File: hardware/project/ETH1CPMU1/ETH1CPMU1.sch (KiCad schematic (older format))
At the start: 0 parts

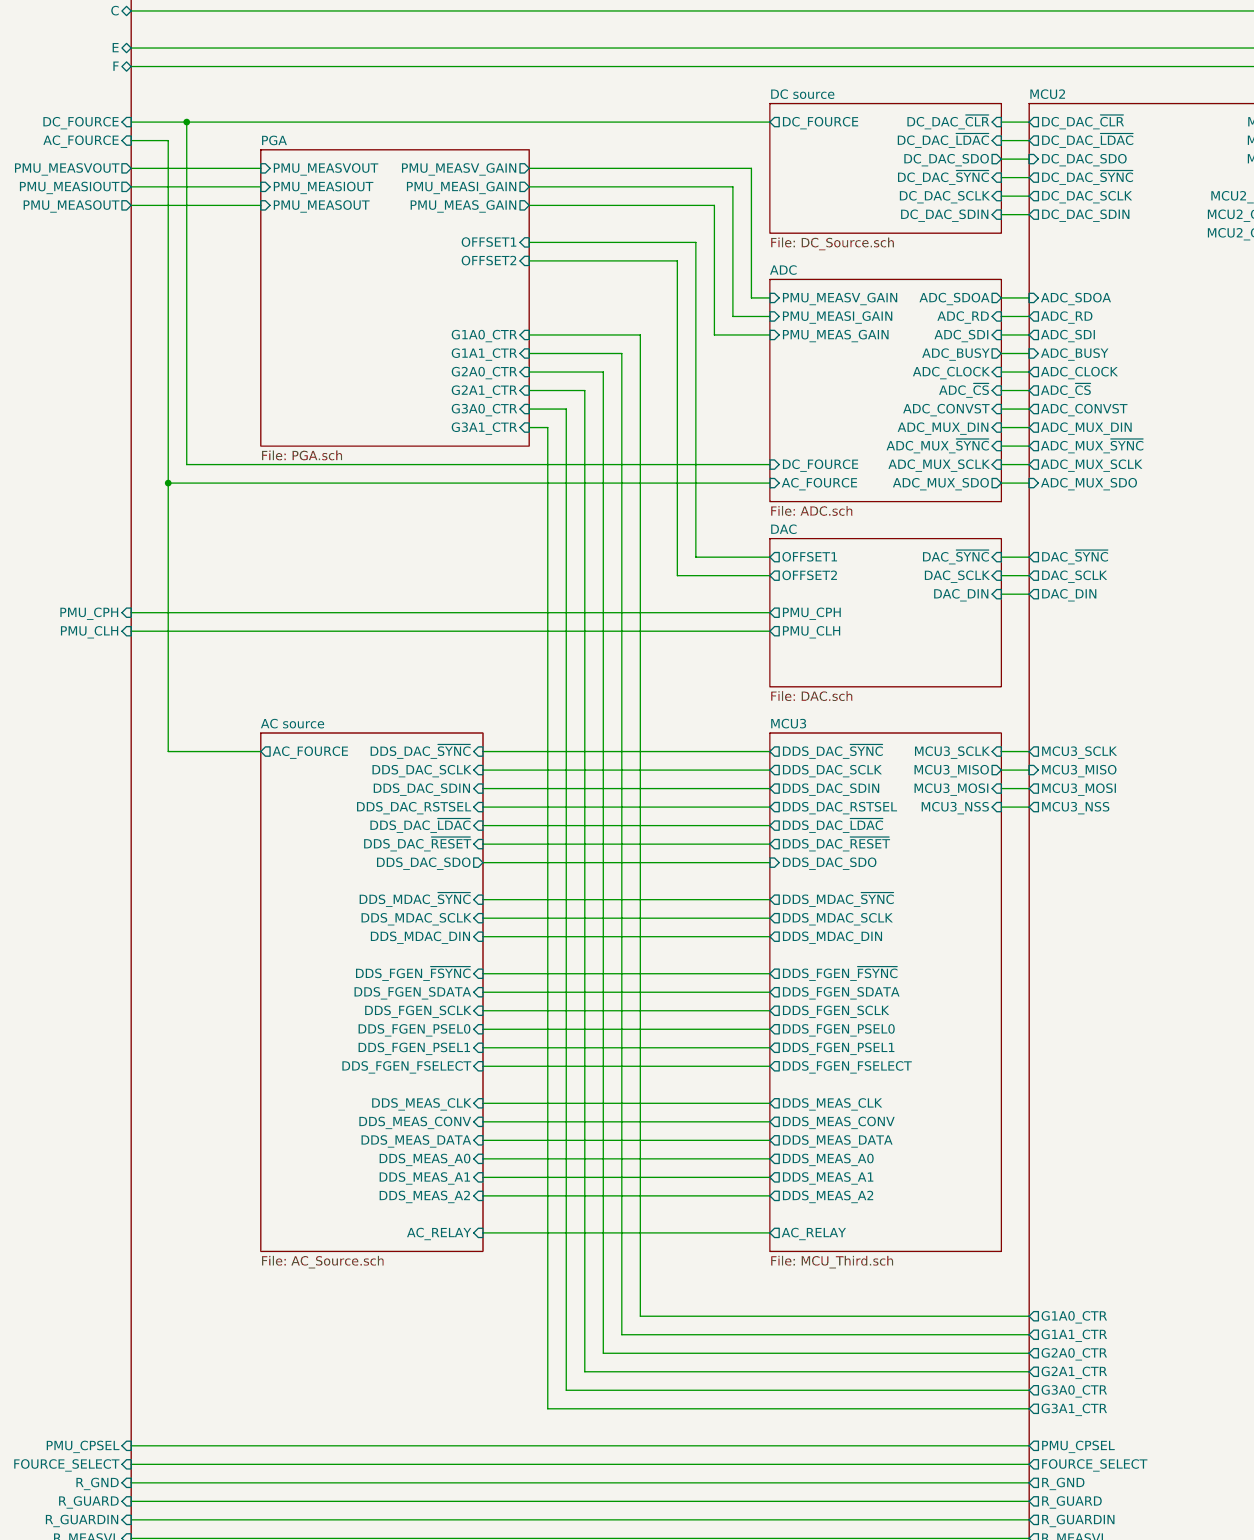
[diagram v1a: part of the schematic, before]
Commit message: Added two analog switches
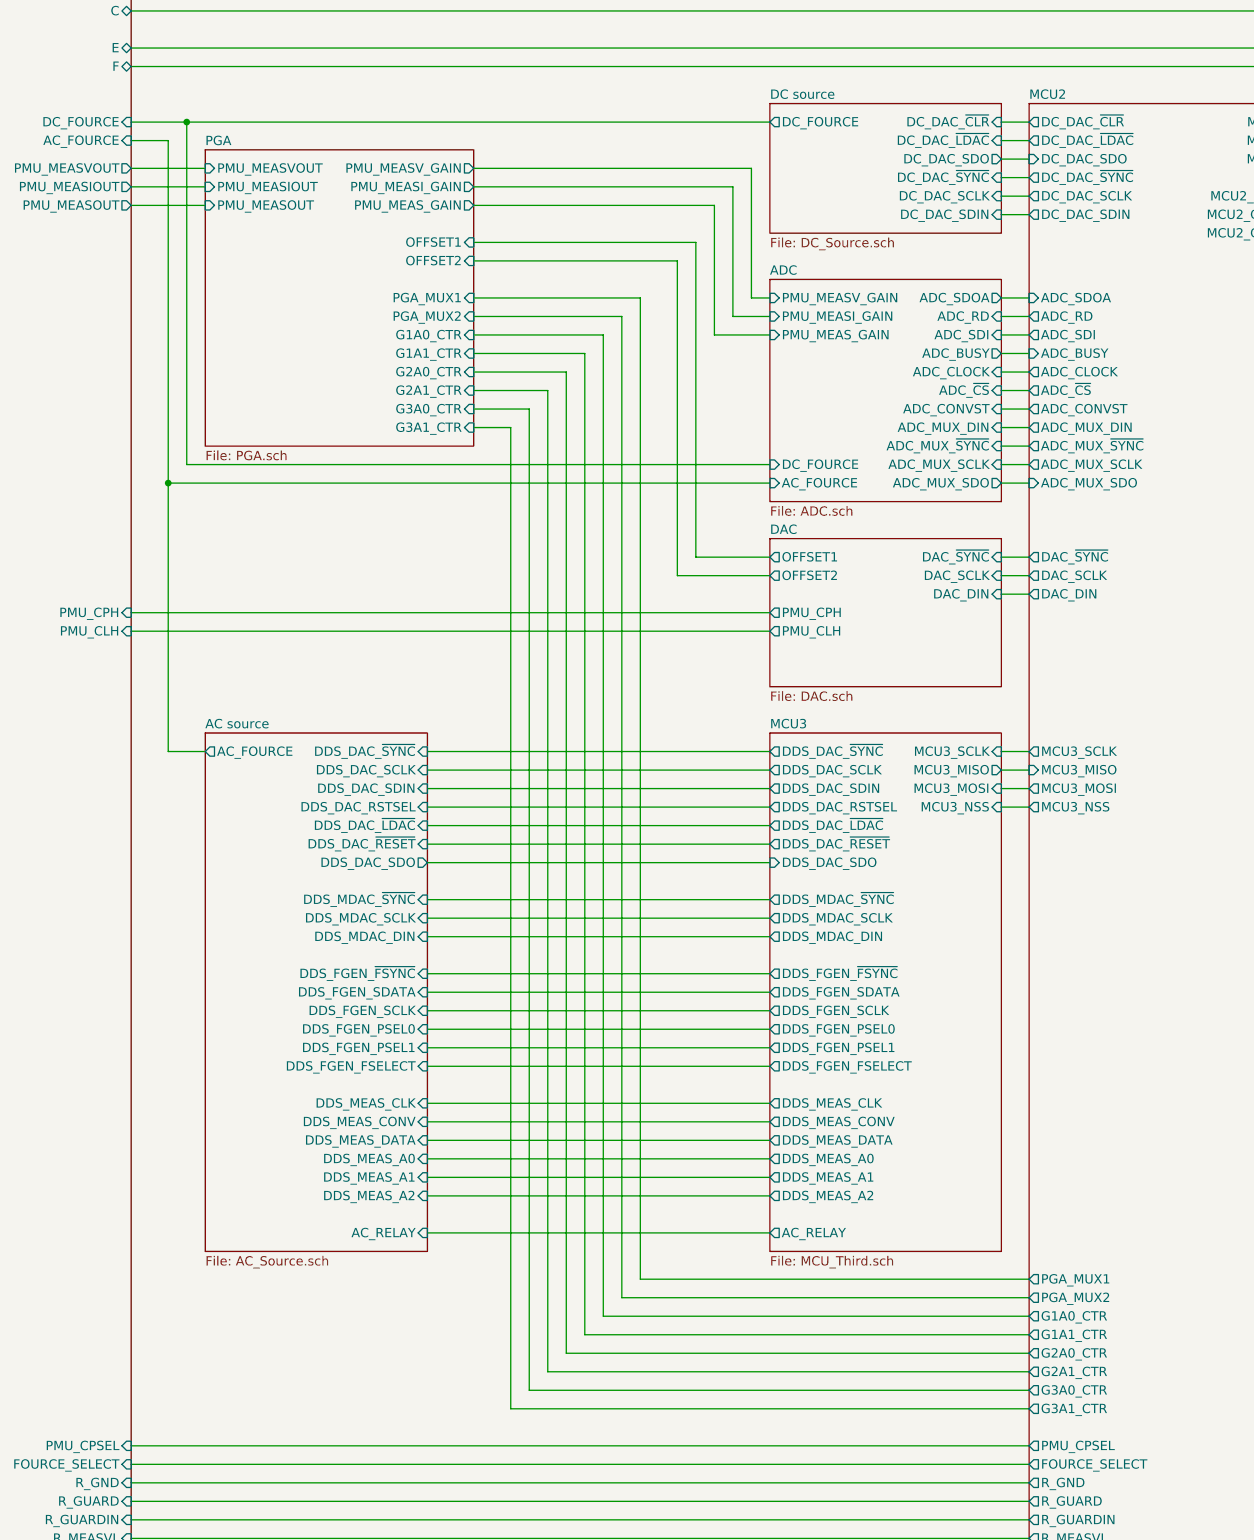
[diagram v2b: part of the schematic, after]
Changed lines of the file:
@@
 $EndSheet
 Wire Wire Line
-	4950 6650 6500 6650
-Wire Wire Line
-	6500 5550 4950 5550
-Wire Wire Line
-	4950 7350 6500 7350
-Wire Wire Line
-	6500 7250 4950 7250
-Wire Wire Line
-	4950 7150 6500 7150
-Wire Wire Line
-	6500 7050 4950 7050
-Wire Wire Line
-	4950 6950 6500 6950
-Wire Wire Line
-	6500 6850 4950 6850
-Wire Wire Line
-	6500 6350 4950 6350
-Wire Wire Line
-	6500 6550 4950 6550
-Wire Wire Line
-	4950 6450 6500 6450
-Wire Wire Line
-	6500 6250 4950 6250
-Wire Wire Line
-	4950 6150 6500 6150
-Wire Wire Line
-	6500 5250 4950 5250
-Wire Wire Line
-	4950 5350 6500 5350
-Wire Wire Line
-	6500 5450 4950 5450
-Wire Wire Line
-	4950 5950 6500 5950
-Wire Wire Line
-	6500 5850 4950 5850
-Wire Wire Line
-	4950 5750 6500 5750
-Wire Wire Line
-	6500 5150 4950 5150
-Wire Wire Line
-	4950 5050 6500 5050
-Wire Wire Line
-	6500 4950 4950 4950
-Wire Wire Line
-	3750 4950 3250 4950
+	4650 6650 6500 6650
+Wire Wire Line
+	6500 5550 4650 5550
+Wire Wire Line
+	4650 7350 6500 7350
+Wire Wire Line
+	6500 7250 4650 7250
+Wire Wire Line
+	4650 7150 6500 7150
+Wire Wire Line
+	6500 7050 4650 7050
+Wire Wire Line
+	4650 6950 6500 6950
+Wire Wire Line
+	6500 6850 4650 6850
+Wire Wire Line
+	6500 6350 4650 6350
+Wire Wire Line
+	6500 6550 4650 6550
+Wire Wire Line
+	4650 6450 6500 6450
+Wire Wire Line
+	6500 6250 4650 6250
+Wire Wire Line
+	4650 6150 6500 6150
+Wire Wire Line
+	6500 5250 4650 5250
+Wire Wire Line
+	4650 5350 6500 5350
+Wire Wire Line
+	6500 5450 4650 5450
+Wire Wire Line
+	4650 5950 6500 5950
+Wire Wire Line
+	6500 5850 4650 5850
+Wire Wire Line
+	4650 5750 6500 5750
+Wire Wire Line
+	6500 5150 4650 5150
+Wire Wire Line
+	4650 5050 6500 5050
+Wire Wire Line
+	6500 4950 4650 4950
+Wire Wire Line
+	3450 4950 3250 4950
 $Sheet
-S 3750 4850 1200 2800
+S 3450 4850 1200 2800
 U 5DF36C25
 F0 "AC source" 50
 F1 "AC_Source.sch" 50
-F2 "AC_FOURCE" O L 3750 4950 50
-F3 "DDS_DAC_~SYNC" I R 4950 4950 50
-F4 "DDS_DAC_SCLK" I R 4950 5050 50
-F5 "DDS_DAC_SDIN" I R 4950 5150 50
-F6 "DDS_MDAC_~SYNC" I R 4950 5750 50
-F7 "DDS_MDAC_SCLK" I R 4950 5850 50
-F8 "DDS_MDAC_DIN" I R 4950 5950 50
-F9 "DDS_DAC_~RESET" I R 4950 5450 50
-F10 "DDS_DAC_~LDAC" I R 4950 5350 50
-F11 "DDS_DAC_RSTSEL" I R 4950 5250 50
-F12 "DDS_FGEN_~FSYNC" I R 4950 6150 50
-F13 "DDS_FGEN_SDATA" I R 4950 6250 50
-F14 "DDS_FGEN_PSEL0" I R 4950 6450 50
-F15 "DDS_FGEN_PSEL1" I R 4950 6550 50
-F16 "DDS_FGEN_SCLK" I R 4950 6350 50
-F17 "DDS_MEAS_CLK" I R 4950 6850 50
-F18 "DDS_MEAS_CONV" I R 4950 6950 50
-F19 "DDS_MEAS_DATA" I R 4950 7050 50
-F20 "DDS_MEAS_A0" I R 4950 7150 50
-F21 "DDS_MEAS_A1" I R 4950 7250 50
-F22 "DDS_MEAS_A2" I R 4950 7350 50
-F23 "DDS_DAC_SDO" O R 4950 5550 50
-F24 "DDS_FGEN_FSELECT" I R 4950 6650 50
-F25 "AC_RELAY" I R 4950 7550 50
+F2 "AC_FOURCE" O L 3450 4950 50
+F3 "DDS_DAC_~SYNC" I R 4650 4950 50
+F4 "DDS_DAC_SCLK" I R 4650 5050 50
+F5 "DDS_DAC_SDIN" I R 4650 5150 50
+F6 "DDS_MDAC_~SYNC" I R 4650 5750 50
+F7 "DDS_MDAC_SCLK" I R 4650 5850 50
+F8 "DDS_MDAC_DIN" I R 4650 5950 50
+F9 "DDS_DAC_~RESET" I R 4650 5450 50
+F10 "DDS_DAC_~LDAC" I R 4650 5350 50
+F11 "DDS_DAC_RSTSEL" I R 4650 5250 50
+F12 "DDS_FGEN_~FSYNC" I R 4650 6150 50
+F13 "DDS_FGEN_SDATA" I R 4650 6250 50
+F14 "DDS_FGEN_PSEL0" I R 4650 6450 50
+F15 "DDS_FGEN_PSEL1" I R 4650 6550 50
+F16 "DDS_FGEN_SCLK" I R 4650 6350 50
+F17 "DDS_MEAS_CLK" I R 4650 6850 50
+F18 "DDS_MEAS_CONV" I R 4650 6950 50
+F19 "DDS_MEAS_DATA" I R 4650 7050 50
+F20 "DDS_MEAS_A0" I R 4650 7150 50
+F21 "DDS_MEAS_A1" I R 4650 7250 50
+F22 "DDS_MEAS_A2" I R 4650 7350 50
+F23 "DDS_DAC_SDO" O R 4650 5550 50
+F24 "DDS_FGEN_FSELECT" I R 4650 6650 50
+F25 "AC_RELAY" I R 4650 7550 50
 $EndSheet
 Wire Wire Line
@@
 	3050 4300 6500 4300
 Wire Wire Line
-	6500 7550 4950 7550
+	6500 7550 4650 7550
 $Sheet
-S 3750 1700 1450 1600
+S 3450 1700 1450 1600
 U 5DED09C5
 F0 "PGA" 50
 F1 "PGA.sch" 50
-F2 "PMU_MEASV_GAIN" O R 5200 1800 50
-F3 "PMU_MEASI_GAIN" O R 5200 1900 50
-F4 "PMU_MEASVOUT" I L 3750 1800 50
-F5 "PMU_MEASIOUT" I L 3750 1900 50
-F6 "G1A0_CTR" I R 5200 2700 50
-F7 "G1A1_CTR" I R 5200 2800 50
-F8 "G2A0_CTR" I R 5200 2900 50
-F9 "G2A1_CTR" I R 5200 3000 50
-F10 "PMU_MEAS_GAIN" O R 5200 2000 50
-F11 "PMU_MEASOUT" I L 3750 2000 50
-F12 "G3A0_CTR" I R 5200 3100 50
-F13 "G3A1_CTR" I R 5200 3200 50
-F14 "OFFSET1" I R 5200 2200 50
-F15 "OFFSET2" I R 5200 2300 50
+F2 "PMU_MEASV_GAIN" O R 4900 1800 50
+F3 "PMU_MEASI_GAIN" O R 4900 1900 50
+F4 "PMU_MEASVOUT" I L 3450 1800 50
+F5 "PMU_MEASIOUT" I L 3450 1900 50
+F6 "G1A0_CTR" I R 4900 2700 50
+F7 "G1A1_CTR" I R 4900 2800 50
+F8 "G2A0_CTR" I R 4900 2900 50
+F9 "G2A1_CTR" I R 4900 3000 50
+F10 "PMU_MEAS_GAIN" O R 4900 2000 50
+F11 "PMU_MEASOUT" I L 3450 2000 50
+F12 "G3A0_CTR" I R 4900 3100 50
+F13 "G3A1_CTR" I R 4900 3200 50
+F14 "OFFSET1" I R 4900 2200 50
+F15 "OFFSET2" I R 4900 2300 50
+F16 "PGA_MUX1" I R 4900 2500 50
+F17 "PGA_MUX2" I R 4900 2600 50
 $EndSheet
 $Sheet
@@
 F60 "G2A0_CTR" O L 7900 8200 50
 F61 "G2A1_CTR" O L 7900 8300 50
+F62 "PGA_MUX1" O L 7900 7800 50
+F63 "PGA_MUX2" O L 7900 7900 50
 $EndSheet
 Wire Wire Line
@@
 	7900 3500 7750 3500
 Wire Wire Line
-	5200 1800 6400 1800
+	4900 1800 6400 1800
 Wire Wire Line
 	6400 1800 6400 2500
@@
 	6400 2500 6500 2500
 Wire Wire Line
-	5200 1900 6300 1900
+	4900 1900 6300 1900
 Wire Wire Line
 	6300 1900 6300 2600
@@
 	6300 2600 6500 2600
 Wire Wire Line
-	5200 2000 6200 2000
+	4900 2000 6200 2000
 Wire Wire Line
 	6200 2000 6200 2700
@@
 	6200 2700 6500 2700
 Wire Wire Line
-	3050 1800 3750 1800
-Wire Wire Line
-	3050 1900 3750 1900
-Wire Wire Line
-	3750 2000 3050 2000
-Wire Wire Line
-	7900 8000 5800 8000
-Wire Wire Line
-	5800 8000 5800 2700
-Wire Wire Line
-	5800 2700 5200 2700
-Wire Wire Line
-	7900 8100 5700 8100
-Wire Wire Line
-	5700 8100 5700 2800
-Wire Wire Line
-	5700 2800 5200 2800
-Wire Wire Line
-	7900 8200 5600 8200
-Wire Wire Line
-	5600 8200 5600 2900
-Wire Wire Line
-	5600 2900 5200 2900
-Wire Wire Line
-	7900 8300 5500 8300
-Wire Wire Line
-	5500 8300 5500 3000
-Wire Wire Line
-	5500 3000 5200 3000
-Wire Wire Line
-	7900 8400 5400 8400
-Wire Wire Line
-	5400 8400 5400 3100
-Wire Wire Line
-	5400 3100 5200 3100
-Wire Wire Line
-	7900 8500 5300 8500
-Wire Wire Line
-	5300 8500 5300 3200
-Wire Wire Line
-	5300 3200 5200 3200
+	3050 1800 3450 1800
+Wire Wire Line
+	3050 1900 3450 1900
+Wire Wire Line
+	3450 2000 3050 2000
+Wire Wire Line
+	7900 8000 5600 8000
+Wire Wire Line
+	5600 8000 5600 2700
+Wire Wire Line
+	5600 2700 4900 2700
+Wire Wire Line
+	7900 8100 5500 8100
+Wire Wire Line
+	5500 8100 5500 2800
+Wire Wire Line
+	5500 2800 4900 2800
+Wire Wire Line
+	7900 8200 5400 8200
+Wire Wire Line
+	5400 8200 5400 2900
+Wire Wire Line
+	5400 2900 4900 2900
+Wire Wire Line
+	7900 8300 5300 8300
+Wire Wire Line
+	5300 8300 5300 3000
+Wire Wire Line
+	5300 3000 4900 3000
+Wire Wire Line
+	7900 8400 5200 8400
+Wire Wire Line
+	5200 8400 5200 3100
+Wire Wire Line
+	5200 3100 4900 3100
+Wire Wire Line
+	7900 8500 5100 8500
+Wire Wire Line
+	5100 8500 5100 3200
+Wire Wire Line
+	5100 3200 4900 3200
 Wire Wire Line
 	6500 3900 6100 3900
@@
 	6100 3900 6100 2200
 Wire Wire Line
-	6100 2200 5200 2200
+	6100 2200 4900 2200
 Wire Wire Line
 	6500 4000 6000 4000
@@
 	6000 4000 6000 2300
 Wire Wire Line
-	6000 2300 5200 2300
+	6000 2300 4900 2300
+Wire Wire Line
+	4900 2600 5700 2600
+Wire Wire Line
+	5700 2600 5700 7900
+Wire Wire Line
+	5700 7900 7900 7900
+Wire Wire Line
+	4900 2500 5800 2500
+Wire Wire Line
+	5800 2500 5800 7800
+Wire Wire Line
+	5800 7800 7900 7800
 $EndSCHEMATC
